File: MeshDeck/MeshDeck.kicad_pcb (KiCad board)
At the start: 2 copper layers, 4 parts, among them CN1 ATGM336H-6N-74, U1 ESP32-S3-WROOM-1(N16R8), U2 SX1262S8S+T-X1, U3 TPS62827ADMQR

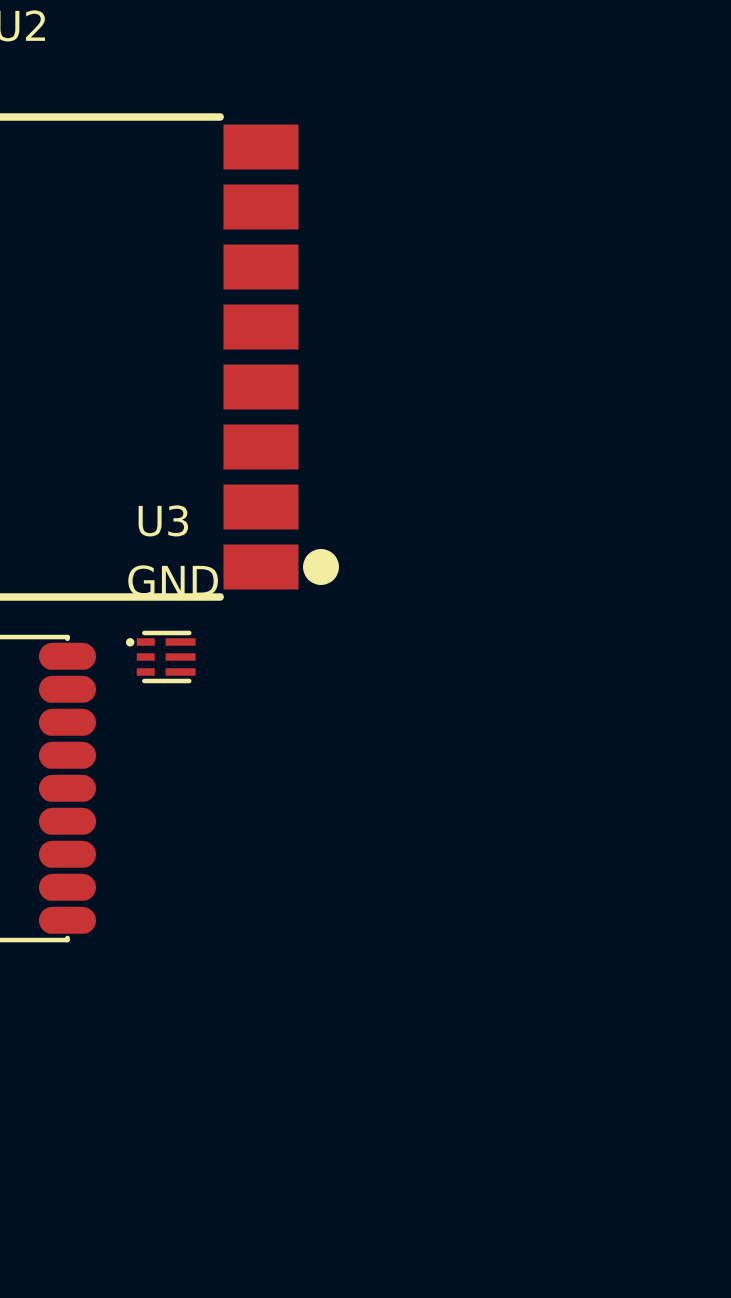
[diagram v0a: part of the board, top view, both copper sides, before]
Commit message: Added ESP-32 and USB stuff
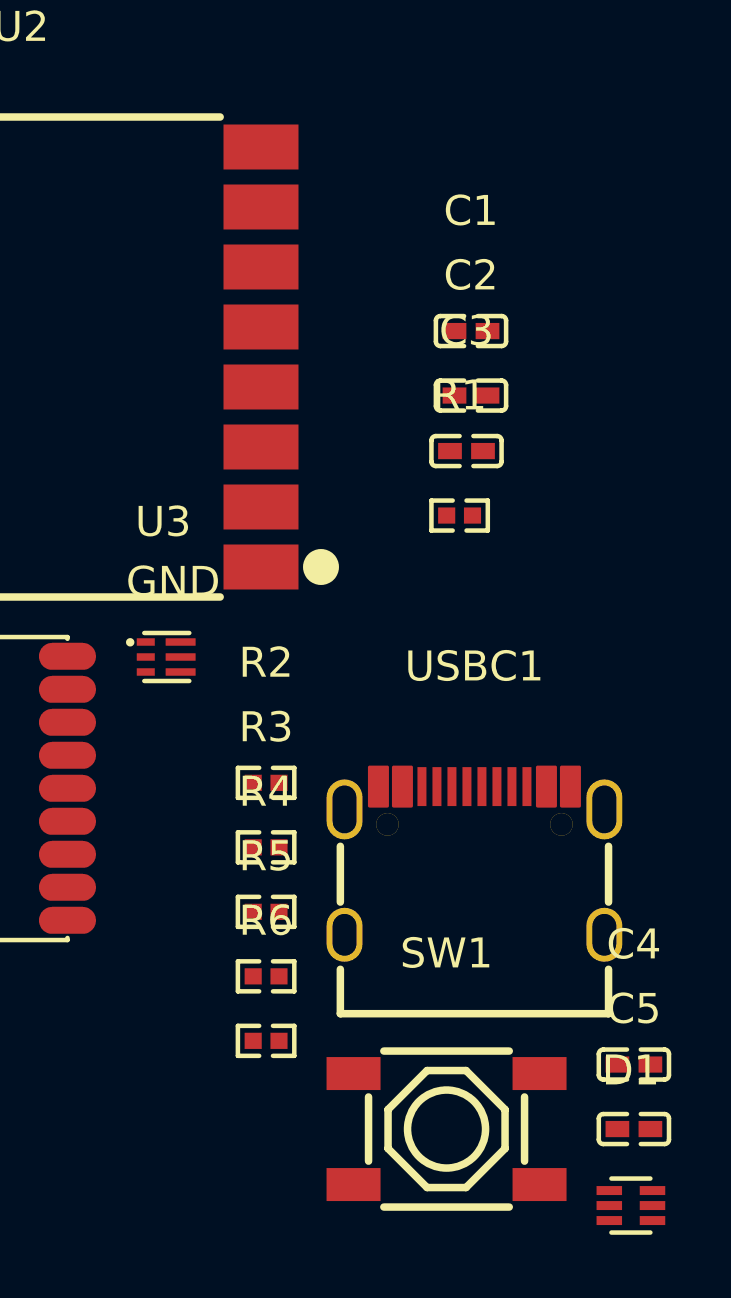
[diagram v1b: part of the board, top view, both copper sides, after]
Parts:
- added C1: 22uF, MeshDeck:C0402, F.Cu at (165.4, 81.3)
- added C2: 0.1uF, MeshDeck:C0402, F.Cu at (165.4, 83.5)
- added C3: 1uF, MeshDeck:C0402, F.Cu at (165.3, 85.3)
- added C4: 0.1uF, MeshDeck:C0402, F.Cu at (170.9, 105.8)
- added C5: 0.1uF, MeshDeck:C0402, F.Cu at (170.9, 108.0)
- added D1: USBLC6-2P6, MeshDeck:SOT-666-6_L1.6-W1.2-P0.50-LS1.6-BR, F.Cu at (170.8, 110.5)
- added R1: 10KOhm, MeshDeck:R0402, F.Cu at (165.1, 87.5)
- added R2: 0 Ohm, MeshDeck:R0402, F.Cu at (158.6, 96.4)
- added R3: 0 Ohm, MeshDeck:R0402, F.Cu at (158.6, 98.6)
- added R4: 0 Ohm, MeshDeck:R0402, F.Cu at (158.6, 100.7)
- added R5: 5.1k, MeshDeck:R0402, F.Cu at (158.6, 102.9)
- added R6: 5.1k, MeshDeck:R0402, F.Cu at (158.6, 105.0)
- added SW1: 4*4*1.7, MeshDeck:SW-SMD_4P-L5.2-W5.2-P3.70-LS6.5, F.Cu at (164.6, 108.0)
- added USBC1: TYPE-C-31-M-12, MeshDeck:USB-C_SMD-TYPE-C-31-M-12_1, F.Cu at (165.6, 99.0)
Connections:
- U1 pad 1: unconnected-(U1-GND-Pad1) -> GND
- U1 pad 13: unconnected-(U1-IO19-Pad13) -> Net-(U1-IO19)
- U1 pad 14: unconnected-(U1-IO20-Pad14) -> Net-(U1-IO20)
- U1 pad 2: unconnected-(U1-3V3-Pad2) -> +3.3V
- U1 pad 3: unconnected-(U1-EN-Pad3) -> /EN
- U1 pad 40: unconnected-(U1-GND-Pad40) -> GND
- U1 pad 41: unconnected-(U1-GND-Pad41) -> GND

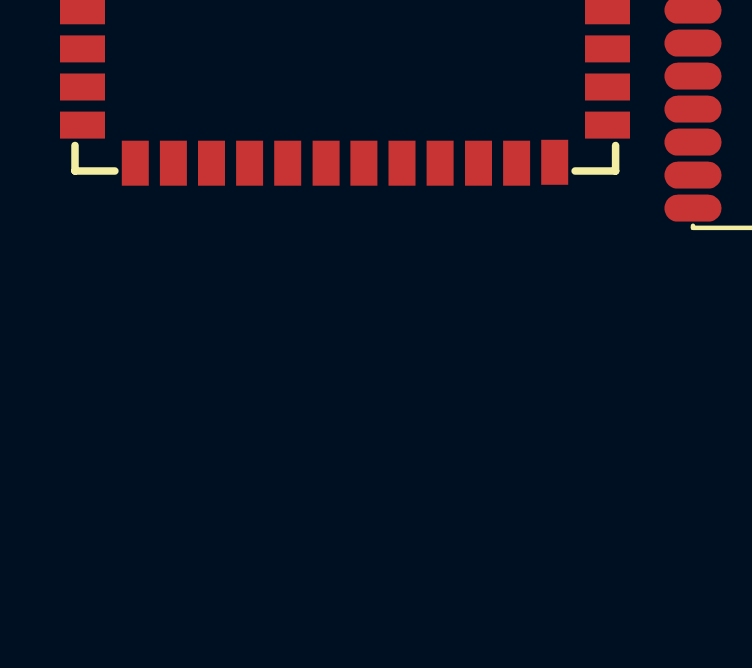
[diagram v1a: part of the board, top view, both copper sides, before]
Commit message: added charging ic circuit
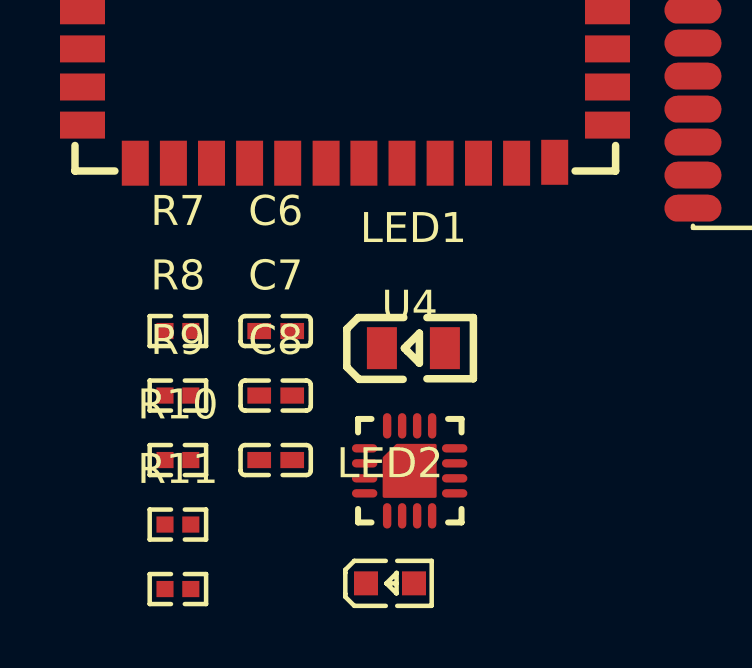
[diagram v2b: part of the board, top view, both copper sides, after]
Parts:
- added C6: 4.7 uF, MeshDeck:C0402, F.Cu at (128.4, 105.1)
- added C7: 1uF, MeshDeck:C0402, F.Cu at (128.4, 107.2)
- added C8: 4.7 uF, MeshDeck:C0402, F.Cu at (128.4, 109.4)
- added LED1: 0805G (Green), MeshDeck:LED0805-R-RD, F.Cu at (133.0, 105.7)
- added LED2: Blue light 0603, MeshDeck:LED0603-RD, F.Cu at (132.2, 113.5)
- added R10: 1.8k, MeshDeck:R0402, F.Cu at (125.1, 111.5)
- added R11: 10K, MeshDeck:R0402, F.Cu at (125.1, 113.7)
- added R7: 1,5K, MeshDeck:R0402, F.Cu at (125.1, 105.1)
- added R8: 1.5K, MeshDeck:R0402, F.Cu at (125.1, 107.2)
- added R9: 1.8k, MeshDeck:R0402, F.Cu at (125.1, 109.4)
- added U4: BQ24074RGTR, MeshDeck:QFN-16_L3.0-W3.0-P0.50-TL-EP1.7, F.Cu at (132.9, 109.8)

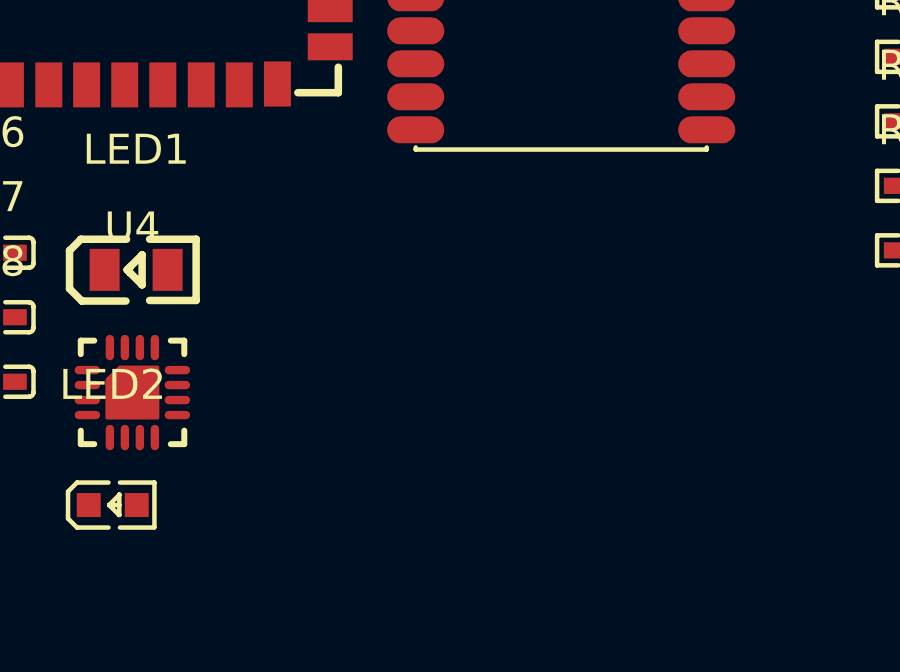
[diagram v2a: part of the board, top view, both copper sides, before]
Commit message: Added 3.3V step down converter
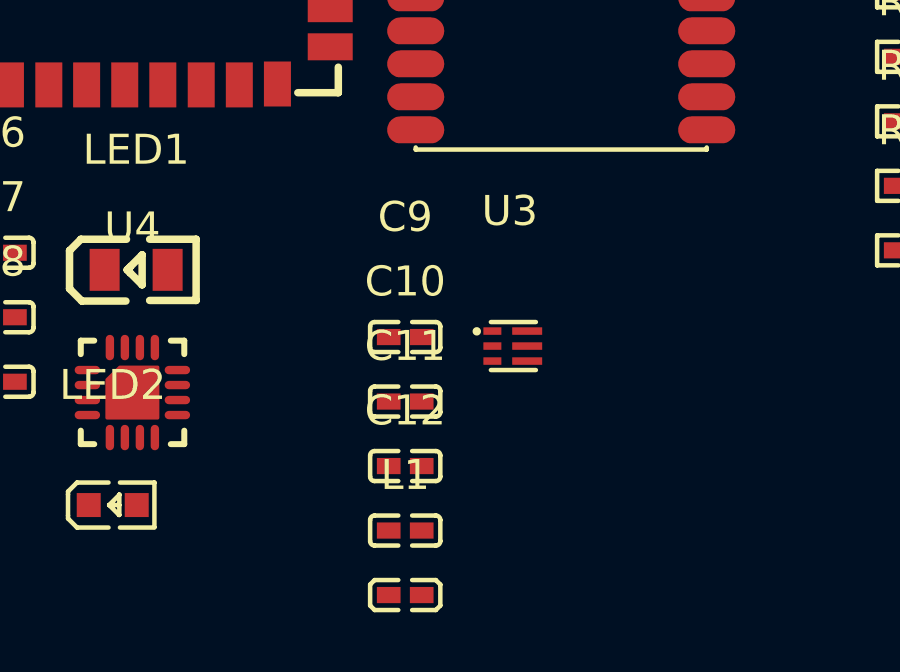
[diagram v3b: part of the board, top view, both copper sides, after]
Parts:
- added C10: 10uF, MeshDeck:C0402, F.Cu at (141.9, 110.0)
- added C11: 10uF, MeshDeck:C0402, F.Cu at (141.9, 112.2)
- added C12: 10uF, MeshDeck:C0402, F.Cu at (141.9, 114.3)
- added C9: 4.7 uF, MeshDeck:C0402, F.Cu at (141.9, 107.9)
- added L1: 0.47 µH, MeshDeck:L0402, F.Cu at (141.9, 116.5)
- added U3: TPS6282533DMQR, MeshDeck:VSON-6_L1.5-W1.5-P0.50-TL, F.Cu at (145.4, 108.2)
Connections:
- C6 pad 1: /OUT -> +3.3V
- R7 pad 2: /OUT -> +3.3V
- R8 pad 2: /OUT -> +3.3V
- U4 pad 10: /OUT -> +3.3V
- U4 pad 11: /OUT -> +3.3V
- U4 pad 6: /OUT -> +3.3V
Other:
- copper layers 2 -> 4

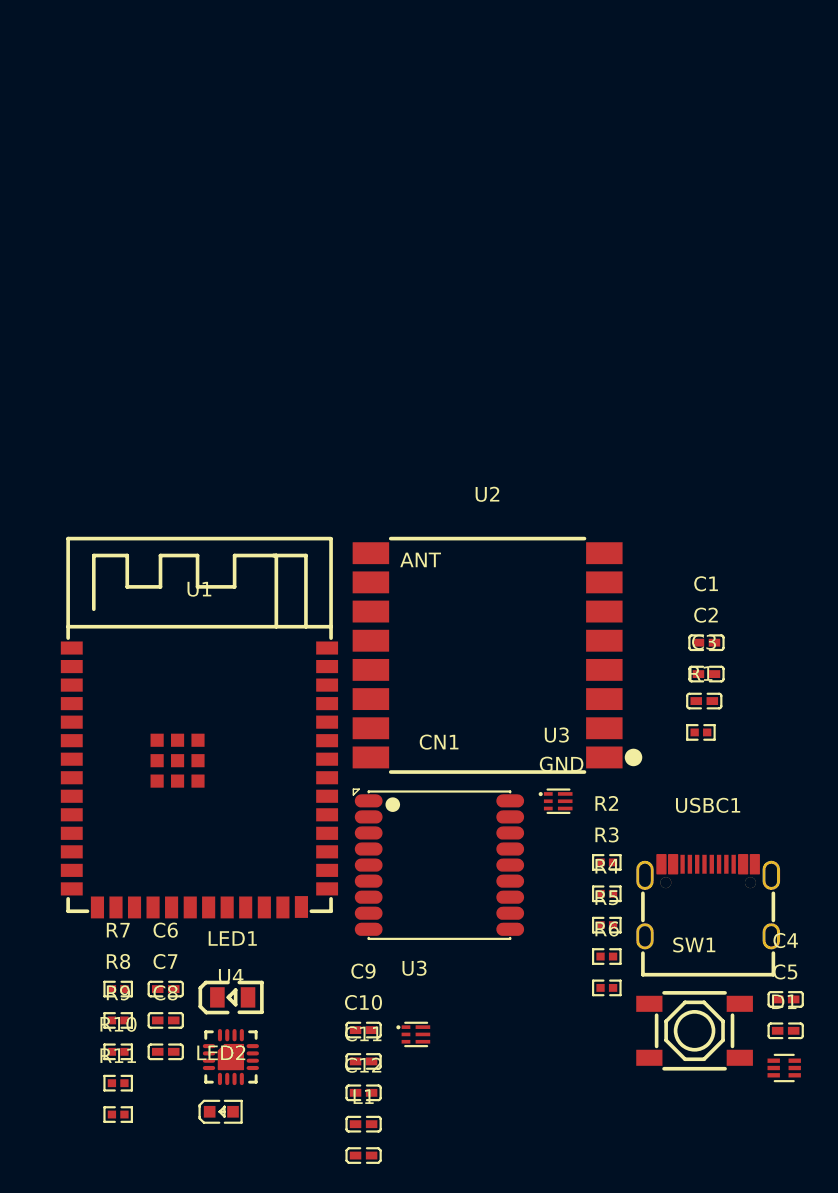
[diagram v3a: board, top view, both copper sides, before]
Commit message: Added oscillator, tidied up with subsheets and added boot btn
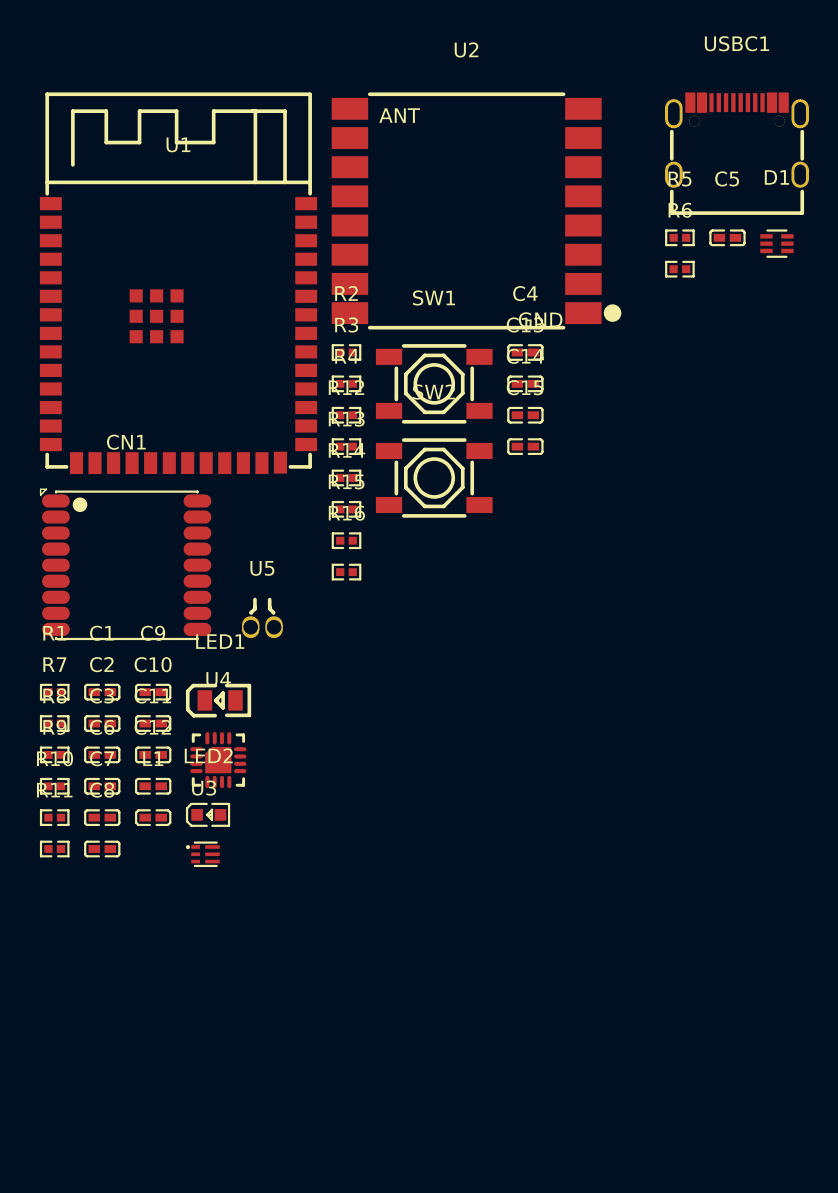
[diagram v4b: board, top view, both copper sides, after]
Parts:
- removed the U3 at (145.4, 108.2)
- removed the U3 at (155.2, 92.2)
- added C13: 0.1uF, MeshDeck:C0402, F.Cu at (153.0, 63.6)
- added C14: 12pF, MeshDeck:C0402, F.Cu at (153.0, 65.8)
- added C15: 12pF, MeshDeck:C0402, F.Cu at (153.0, 67.9)
- added R12: 0 Ohm, MeshDeck:R0402, F.Cu at (140.8, 67.9)
- added R13: 10KOhm, MeshDeck:R0402, F.Cu at (140.8, 70.1)
- added R14: 0 Ohm, MeshDeck:R0402, F.Cu at (140.8, 72.2)
- added R15: 0 Ohm, MeshDeck:R0402, F.Cu at (140.8, 74.4)
- added R16: 10k, MeshDeck:R0402, F.Cu at (140.8, 76.5)
- added SW2: 4*4*1.7, MeshDeck:SW-SMD_4P-L5.2-W5.2-P3.70-LS6.5, F.Cu at (146.8, 70.1)
- added U3: TPS6282533DMQR, MeshDeck:VSON-6_L1.5-W1.5-P0.50-TL, F.Cu at (131.0, 95.8)
- added U5: RN32768114, MeshDeck:OSC-TH_BD2.0-P0.50, F.Cu at (135.0, 80.3)
- moved D1 56.5 mm to (170.3, 54.0)
- moved C5 54.5 mm to (166.9, 53.6)
- moved USBC1 52.2 mm to (167.5, 46.8)
- moved R6 49.5 mm to (163.6, 55.8)
- moved R5 49.5 mm to (163.6, 53.6)
- moved SW1 47.8 mm to (146.8, 63.6)
- moved C4 47.8 mm to (153.0, 61.5)
- moved R1 44.4 mm to (120.8, 84.7)
- moved C1 41.5 mm to (124.0, 84.7)
- moved C2 41.5 mm to (124.0, 86.9)
- moved C3 41.4 mm to (124.0, 89.0)
- moved R3 39.2 mm to (140.8, 63.6)
- moved R2 39.2 mm to (140.8, 61.5)
- moved R4 39.2 mm to (140.8, 65.8)
- moved U1 30.5 mm to (129.3, 60.1)
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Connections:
- net /BAT renamed /Power Sheet/BAT
- net /CC1 renamed /USBSheet/CC1
- net /CC2 renamed /USBSheet/CC2
- net /VBUS renamed /USBSheet/VBUS
- C1 pad 1: +3.3V -> /3V3
- C10 pad 2: +3.3V -> /3V3
- C11 pad 2: +3.3V -> /3V3
- C12 pad 2: +3.3V -> /3V3
- C2 pad 1: +3.3V -> /3V3
- C6 pad 1: +3.3V -> /Power Sheet/BCC_OUT
- C9 pad 1: +3.3V -> /Power Sheet/BCC_OUT
- D1 pad 4: /USB_D- -> /USB_D+
- D1 pad 6: /USB_D+ -> /USB_D-
- L1 pad 2: unconnected-(L1-Pad2) -> /3V3
- R1 pad 2: +3.3V -> /3V3
- R7 pad 2: +3.3V -> /Power Sheet/BCC_OUT
- R8 pad 2: +3.3V -> /Power Sheet/BCC_OUT
- U1 pad 2: +3.3V -> /3V3
- U1 pad 27: unconnected-(U1-IO0-Pad27) -> /IO0
- U1 pad 8: unconnected-(U1-IO15-Pad8) -> Net-(U1-IO15)
- U1 pad 9: unconnected-(U1-IO16-Pad9) -> Net-(U1-IO16)
- U4 pad 10: +3.3V -> /Power Sheet/BCC_OUT
- U4 pad 11: +3.3V -> /Power Sheet/BCC_OUT
- U4 pad 6: +3.3V -> /Power Sheet/BCC_OUT

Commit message: set up LoRa module and screen (wip)
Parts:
- added C16: 1uF, MeshDeck:C0402, F.Cu at (153.0, 102.6)
- added C17: 1Nf, MeshDeck:C0402, F.Cu at (153.0, 104.7)
- added RF1: HJ-SMA023, MeshDeck:SMA-SMD_HJ-SMA023, F.Cu at (147.2, 104.8)
- added U6: ~, MeshDeck:2.8 SPI LCD TFT ST7789, F.Cu at (114.4, 69.3)
- moved U5 56.6 mm to (155.7, 133.0)
- moved CN1 56.6 mm to (146.4, 128.8)
- moved U3 56.0 mm to (174.6, 60.7)
- moved C11 56.0 mm to (171.1, 53.9)
- moved L1 56.0 mm to (171.1, 58.2)
- moved LED2 56.0 mm to (174.9, 58.0)
- moved R10 56.0 mm to (164.3, 58.2)
- moved R8 56.0 mm to (164.3, 53.9)
- moved U4 56.0 mm to (175.5, 54.2)
- moved C10 56.0 mm to (171.1, 51.7)
- moved C12 56.0 mm to (171.1, 56.0)
- moved C3 56.0 mm to (167.6, 53.9)
- moved C7 56.0 mm to (167.6, 58.2)
- moved C9 56.0 mm to (171.1, 49.6)
- moved LED1 56.0 mm to (175.7, 50.1)
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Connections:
- U1 pad 10: unconnected-(U1-IO17-Pad10) -> /IO17
- U1 pad 17: unconnected-(U1-IO9-Pad17) -> /IO9
- U1 pad 19: unconnected-(U1-IO11-Pad19) -> /IO11
- U1 pad 20: unconnected-(U1-IO12-Pad20) -> /IO12
- U1 pad 21: unconnected-(U1-IO13-Pad21) -> /IO13
- U1 pad 22: unconnected-(U1-IO14-Pad22) -> /IO14
- U1 pad 26: unconnected-(U1-IO45-Pad26) -> /IO45
- U1 pad 32: unconnected-(U1-IO39-Pad32) -> /SPI.SCK
- U1 pad 33: unconnected-(U1-IO40-Pad33) -> /SPI.MISO
- U1 pad 34: unconnected-(U1-IO41-Pad34) -> /SPI.MOSI
- U1 pad 35: unconnected-(U1-IO42-Pad35) -> /IO42
- U2 pad 1: unconnected-(U2-GND-Pad1) -> GND
- U2 pad 10: unconnected-(U2-GND-Pad10) -> GND
- U2 pad 11: unconnected-(U2-RXE-Pad11) -> /IO14
- U2 pad 13: unconnected-(U2-VCC-Pad13) -> /3V3
- U2 pad 15: unconnected-(U2-DIO1-Pad15) -> /IO45
- U2 pad 16: unconnected-(U2-BUSY-Pad16) -> /IO13
- U2 pad 2: unconnected-(U2-SO-Pad2) -> /SPI.MISO
- U2 pad 3: unconnected-(U2-SI-Pad3) -> /SPI.MOSI
- U2 pad 4: unconnected-(U2-SCK-Pad4) -> /SPI.SCK
- U2 pad 5: unconnected-(U2-NSS-Pad5) -> /IO9
- U2 pad 6: unconnected-(U2-RST-Pad6) -> /IO17
- U2 pad 8: unconnected-(U2-GND-Pad8) -> GND
- U2 pad 9: unconnected-(U2-ANT-Pad9) -> Net-(RF1-SIG)
